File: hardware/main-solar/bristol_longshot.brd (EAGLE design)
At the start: 14 x 64 mm, 72 parts, among them U1 SAM_D20E, U2 SI4060, U3 UBLOX_MAX, U4 S25FS-S, U44 AD8354, U5 TG-5006CJ, U6 TG-5006CJ, U7 TPS3123, U8 SN74LVC1G32DCKR, U9 SE880, Y1 ABS05

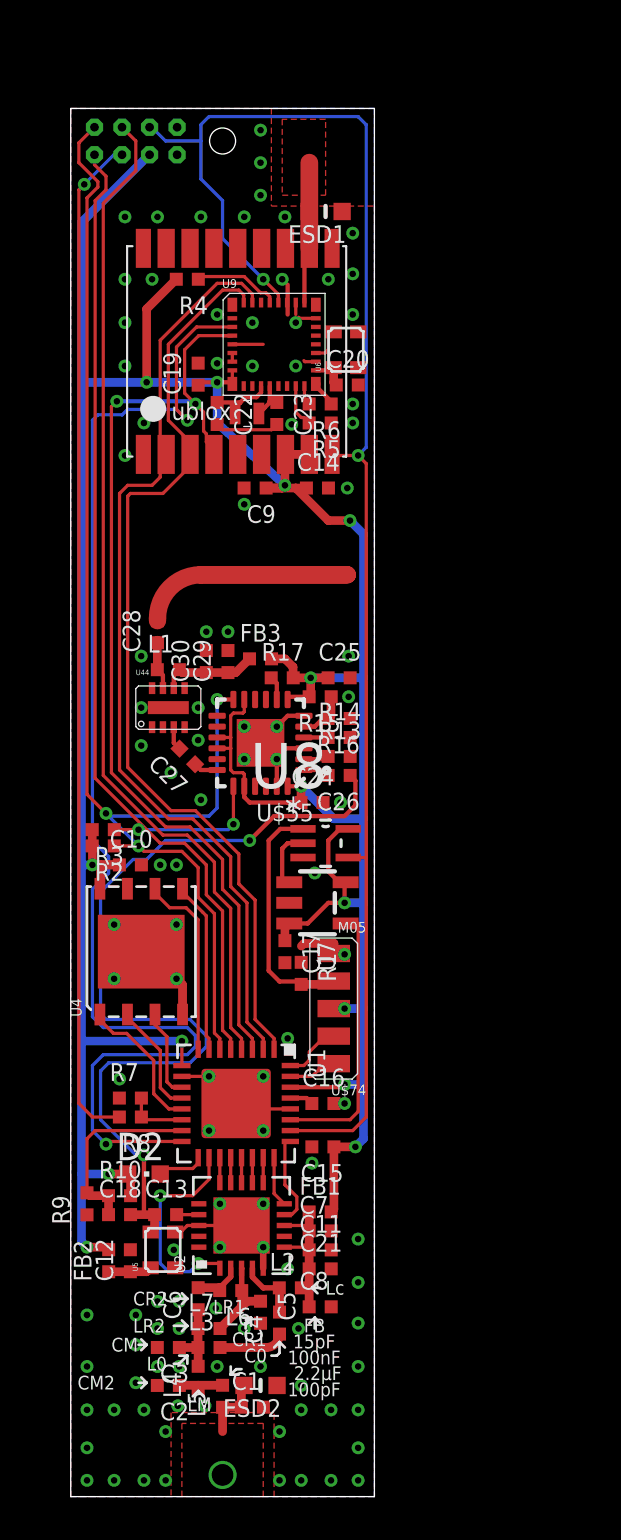
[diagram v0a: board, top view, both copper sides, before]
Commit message: Moved to single-board solar tracker. Parts lists out of date!
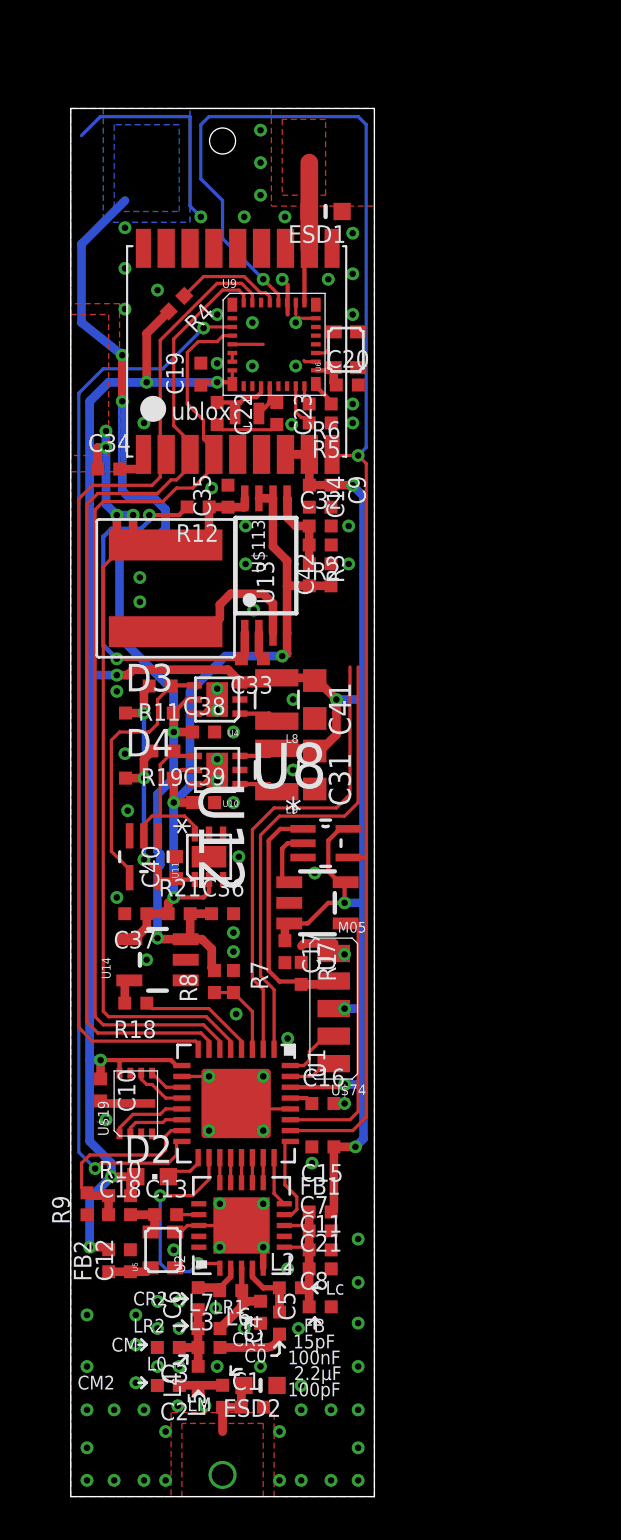
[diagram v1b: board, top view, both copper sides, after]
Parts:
- removed C24, C25, C26, C27, C28, C29: 100nF, microbuilder_v3:_0402
- removed C30: 100pF, microbuilder_v3:_0402
- removed FB3: (no value), microbuilder_v3:_0402
- removed L1: 100nH, microbuilder_v3:_0402
- removed R13, R14: 0Ω, microbuilder_v3:_0402
- removed R15, R17: 10kΩ, microbuilder_v3:_0402
- removed R16: 15kΩ, microbuilder_v3:_0402
- removed U$51: M04X2, fbri:M04X2
- removed U$55: SI5356, si5356:QFN24_4MM
- removed U44: AD8354, fbri:LFCSP_VD_8
- added C31, C41: 10µF, resistor:C0603K
- added C32, C33, C40: 1nF, microbuilder_v3:_0402
- added C34, C35, C36, C37, C38, C39, C42: 4.7µF, microbuilder_v3:_0402
- added D3, D4: BAT760, BAT760:SOD323
- added L8, L9: 2.2µH, SparkFun:1007
- added R11, R19: 10kΩ, microbuilder_v3:_0402
- added R12: 1kΩ, microbuilder_v3:_0402
- added R18: 2.2kΩ, microbuilder_v3:_0402
- added R21: DNP, microbuilder_v3:_0402
- added U$113: XAL6060, XAL6060:XAL60
- added U$19: SST25WF040BT-40I/NP, fbri:USON-8
- added U10: TPS62243, TPS62243:S-PWSON-N6
- added U11: TPS3808, TPS3808:S-PWSON-N6
- added U12: 74LVC1G04GW, 74LVC1G04GW_inverter:SOT65P210X110-5N
- added U13: SPV1040, spv1040:TSSOP8
- added U14: LT4054ES5-4.2, XYKlib:SOT23-5
- R2: value 10kΩ -> 82kΩ
- R3: value 10kΩ -> 220kΩ
- U4: value S25FS-S -> TPS62243; device fbri:WSON8 -> TPS62243:S-PWSON-N6
- moved R2 17.1 mm to (11.5, 43.9)
- moved R3 15.1 mm to (11.0, 42.5), turned to 270 degrees
- moved U4 12.1 mm to (6.75, 36.8)
- moved C10 10.5 mm to (1.38, 18.8), turned to 270 degrees
- moved R8 7.35 mm to (6.62, 23.8), turned to 90 degrees
- moved R7 7.17 mm to (7.50, 23.8), turned to 270 degrees
- moved C9 3.52 mm to (12.0, 46.1), turned to 270 degrees
- moved R4 1.23 mm to (4.88, 55.0), turned to 225 degrees
- moved C14 0.53 mm to (11.0, 46.1), turned to 270 degrees
- moved D2 0.40 mm to (3.75, 14.8)
- moved C19 0.12 mm to (6.00, 51.8)
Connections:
- net N$2 renamed SE_VREG
- net N$4 renamed SE_MODE_PULL
- net TANK renamed RF_TANK
- removed net 1.2V: R8.2, U$51.P$5
- removed net AMPL_OUT: C28.1, L1.1, U44.7
- removed net AMPL_VPOS: C29.1, C30.1, FB3.1, L1.2, U44.6
- removed net CLKIN: R14.1, U$55.4
- removed net HF_ANT: C28.2
- removed net HF_CLK: C27.1, U$55.18
- removed net INPT: C27.2, U44.3
- removed net INTR: R17.1, U$55.8
- removed net N$7: U$55.9
- removed net SSC_DIS: R15.1, R16.2, U$55.5
- removed net XA: C26.2, U$55.1
- removed net XB: R13.1, U$55.2
- new net BATTERY: C36.1, C38.1, D3.A, R21.2, R8.2, U14.3, U4.5
- new net BATTERY_BUCK_SW: L8.1, U4.1
- new net BATTERY_EN: R11.1, U12.4, U4.4
- new net CHG_CONTROL: R18.1, U1.4
- new net CHG_STATUS: U14.1
- new net CT: U11.3
- new net LX1: U$113.P$2, U13.3
- new net MPP-SET: C33.2, R12.2, U13.1
- new net MPPT-VOUT-TANK: C37.1, C39.1, C42.1, D4.A, R21.1, R3.2, U10.5, U11.2, U13.4, U13.6, U13.7, U14.4
- new net PROG: R18.2, U14.5
- new net SPV_VCTRL1: C32.1, R2.2, R3.1, U13.5
- new net SUPERVISOR_VCC: C40.1, D3.C, D4.C, R11.2, R19.2, U11.1, U12.5
- new net TANK_BUCK_SW: L9.1, U10.1
- new net TANK_EN: R19.1, U10.4, U11.6, U12.2
- net !RESET: no longer U$51.P$4
- net 1.8V: now also C31.1, C41.1, L8.2, L9.2, U$19.8, U10.3, U4.3; no longer C24.1, C25.1, FB3.2, R15.2, R17.2, R2.2, R3.2, U$51.P$3, U$55.11, U$55.15, U$55.16, U$55.20, U$55.24, U$55.7, U4.8
- net GIMO: now also U1.7; no longer U1.1
- net GND: now also C31.2, C32.2, C33.1, C34.2, C35.2, C36.2, C37.2, C38.2, C39.2, C40.2, C41.2, C42.2, R2.1, U$19.4, U$19.P$9, U10.2, U10.6, U10.PAD, U11.5, U11.PAD, U12.3, U13.2, U14.2, U4.2, U4.6; no longer C24.2, C25.2, C29.2, C30.2, R13.2, R14.2, R16.1, U$51.P$1, U$51.P$2, U$55.23, U$55.3, U$55.6, U$55.PAD, U4.4, U44.1, U44.4, U44.5, U44.8, U44.EPAD
- net GOMI: now also U1.8; no longer U1.2
- net MEM_CSN: now also U$19.1; no longer U4.1
- net MEM_MISO: now also U$19.2, U1.14; no longer U1.12, U4.2
- net MEM_MOSI: now also U$19.5, U1.11; no longer U1.7, U4.5
- net MEM_SCK: now also U$19.6, U1.12; no longer U1.8, U4.6
- net MEM_WPN: now also U$19.3; no longer U1.11, U4.3
- net SCL: now also U1.2; no longer R2.1, U$51.P$8, U$55.12, U1.6
- net SDA: now also U1.1; no longer R3.1, U$51.P$7, U$55.19, U1.5
- net TCXO_OUT: no longer C26.1
- net TIMEPULSE: now also U1.6; no longer U1.3
- net VBATT_SENSE: now also U1.3; no longer U1.14
- net VSOLAR: now also C34.1, C35.1, R12.1, U$113.P$1, U1.5, U13.8; no longer U$51.P$6, U1.4
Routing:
- net BATTERY: track 0.00 -> 49.3 mm, vias 0 -> 4
- net 1.2V: track 46.9 -> 0.00 mm, vias 1 -> 0
- net TCXO_OUT: track 41.8 -> 2.48 mm, vias 2 -> 0
- net SCL: track 59.1 -> 21.4 mm, vias 3 -> 0
- net MPPT-VOUT-TANK: track 0.00 -> 34.0 mm, vias 0 -> 3
- net SDA: track 52.6 -> 21.5 mm, vias 2 -> 0
- net 1.8V: track 166.2 -> 136.6 mm, vias 14 -> 12
- net MPP-SET: track 0.00 -> 17.5 mm, vias 0 -> 2
- net HF_ANT: track 16.4 -> 0.00 mm
- net SUPERVISOR_VCC: track 0.00 -> 14.1 mm, vias 0 -> 3
- net BATTERY_EN: track 0.00 -> 12.2 mm
- net SE_ON_OFF: track 57.6 -> 49.3 mm
- net TANK_EN: track 0.00 -> 8.03 mm
- net LX1: track 0.00 -> 7.58 mm
- net MEM_SCK: track 8.96 -> 2.51 mm
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- added copper zone on layer 16, net BATTERY
- added copper zone on layer 1, net VSOLAR
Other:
- board text added: "+vbat"
- board text added: "-vbat"
- board text added: "V0.981.0"
- board text removed: "V0.98.0"

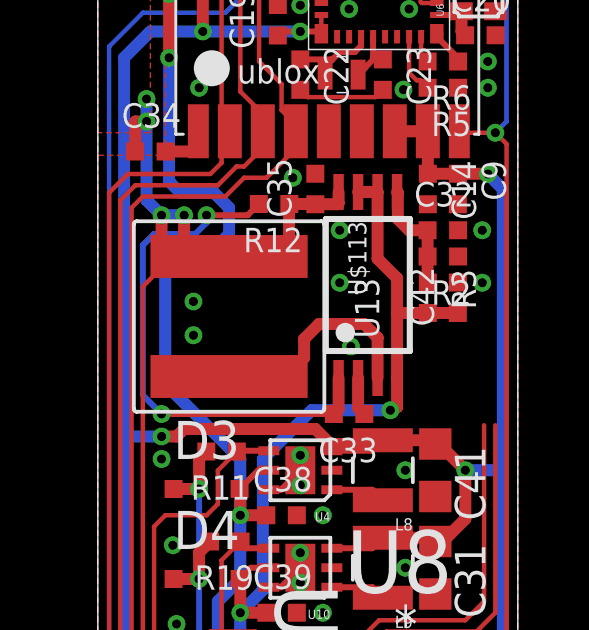
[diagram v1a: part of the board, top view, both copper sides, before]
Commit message: Added LPS3015 mppt inductor footprint alongside XAL6060 footprint
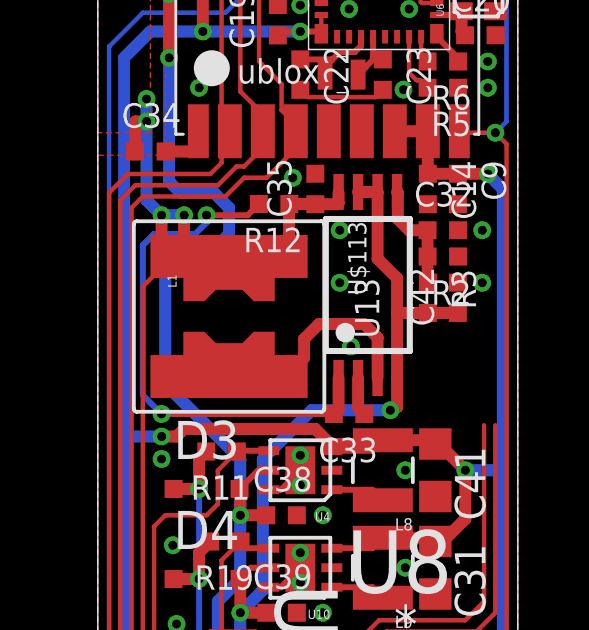
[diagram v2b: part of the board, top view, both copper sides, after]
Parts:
- added L1: 10uH LPS3015, PecanFemto4:LPS3015
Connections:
- net LX1: now also L1.2_1, L1.2_2, L1.2_3, L1.2_4, L1.2_5, L1.2_6, L1.2_7, L1.2_8, L1.2_9
- net VSOLAR: now also L1.1_1, L1.1_2, L1.1_3, L1.1_4, L1.1_5, L1.1_6, L1.1_7, L1.1_8, L1.1_9
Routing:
- net LX1: track 7.58 -> 12.8 mm
- net VSOLAR: track 47.9 -> 52.6 mm
- net GND: vias 107 -> 105
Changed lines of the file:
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@@
 <setting verticaltext="up"/>
 </settings>
-<grid distance="0.125" unitdist="mm" unit="mm" style="lines" multiple="1" display="yes" altdistance="0.025" altunitdist="inch" altunit="inch"/>
+<grid distance="1" unitdist="mm" unit="mm" style="lines" multiple="1" display="yes" altdistance="0.025" altunitdist="inch" altunit="inch"/>
 <layers>
 <layer number="1" name="Top" color="4" fill="1" visible="yes" active="yes"/>
@@
 <layer number="54" name="bGND_GNDA" color="1" fill="9" visible="no" active="no"/>
 <layer number="56" name="wert" color="7" fill="1" visible="no" active="no"/>
+<layer number="57" name="tCAD" color="7" fill="1" visible="no" active="no"/>
 <layer number="90" name="Modules" color="5" fill="1" visible="no" active="no"/>
 <layer number="91" name="Nets" color="2" fill="1" visible="no" active="no"/>
@@
 <layer number="97" name="Info" color="7" fill="1" visible="no" active="no"/>
 <layer number="98" name="Guide" color="6" fill="1" visible="no" active="no"/>
+<layer number="99" name="SpiceOrder" color="7" fill="1" visible="no" active="no"/>
 <layer number="100" name="Muster" color="7" fill="1" visible="no" active="no"/>
 <layer number="101" name="Patch_Top" color="12" fill="4" visible="yes" active="yes"/>
@@
 <layer number="132" name="bAdjust" color="7" fill="1" visible="yes" active="yes"/>
 <layer number="144" name="Drill_legend" color="7" fill="1" visible="yes" active="yes"/>
+<layer number="150" name="Notes" color="7" fill="1" visible="yes" active="yes"/>
 <layer number="151" name="HeatSink" color="7" fill="1" visible="yes" active="yes"/>
 <layer number="152" name="_bDocu" color="7" fill="1" visible="yes" active="yes"/>
+<layer number="153" name="FabDoc1" color="7" fill="1" visible="yes" active="yes"/>
+<layer number="154" name="FabDoc2" color="7" fill="1" visible="yes" active="yes"/>
+<layer number="155" name="FabDoc3" color="7" fill="1" visible="yes" active="yes"/>
 <layer number="199" name="Contour" color="7" fill="1" visible="yes" active="yes"/>
 <layer number="200" name="200bmp" color="1" fill="10" visible="yes" active="yes"/>
@@
 <element name="C42" library="microbuilder_v3" package="_0402" value="4.7µF" x="12" y="42.5" rot="R90"/>
 <element name="R21" library="microbuilder_v3" package="_0402" value="DNP" x="5" y="26.875"/>
+<element name="L1" library="PecanFemto4" package="LPS3015" value="10uH LPS3015" x="4.375" y="41.875" rot="R270"/>
 </elements>
 <signals>
@@
 <via x="8.0625" y="44.75" extent="1-16" drill="0.3"/>
 <via x="8.0625" y="43" extent="1-16" drill="0.3"/>
-<via x="3.1875" y="42.375" extent="1-16" drill="0.3"/>
-<via x="3.1875" y="41.25" extent="1-16" drill="0.3"/>
 <via x="8.4375" y="40.875" extent="1-16" drill="0.3"/>
 <wire x1="5.5" y1="63.625" x2="1.375" y2="63.625" width="0.15" layer="16"/>
@@
 <wire x1="6.375" y1="45.617" x2="6.375" y2="44" width="0.4" layer="1"/>
 <wire x1="6.375" y1="44" x2="6.25" y2="43.875" width="0.4" layer="1"/>
-<wire x1="6.25" y1="43.875" x2="4.375" y2="43.875" width="0.4" layer="1"/>
+<wire x1="6.25" y1="43.875" x2="6" y2="43.875" width="0.4" layer="1"/>
+<wire x1="6" y1="43.875" x2="4.375" y2="43.875" width="0.4" layer="1"/>
 <wire x1="7.25" y1="45.617" x2="7.992" y2="45.617" width="0.4" layer="1"/>
 <wire x1="7.992" y1="45.617" x2="8.025" y2="45.65" width="0.4" layer="1"/>
@@
 <vertex x="0" y="48"/>
 </polygon>
+<contactref element="L1" pad="1_5"/>
+<contactref element="L1" pad="1_6"/>
+<contactref element="L1" pad="1_9"/>
+<contactref element="L1" pad="1_8"/>
+<contactref element="L1" pad="1_3"/>
+<contactref element="L1" pad="1_2"/>
+<contactref element="L1" pad="1_1"/>
+<contactref element="L1" pad="1_4"/>
+<contactref element="L1" pad="1_7"/>
+<wire x1="4.375" y1="43.875" x2="4.375" y2="43.145" width="0.2" layer="1"/>
+<wire x1="5.75" y1="43.375" x2="5.75" y2="42.8495" width="0.2" layer="1"/>
+<wire x1="5.75" y1="42.8495" x2="5.772" y2="42.8275" width="0.2" layer="1"/>
+<wire x1="5.772" y1="42.8275" x2="5.261459375" y2="42.8275" width="0.2" layer="1"/>
+<wire x1="5.261459375" y1="42.8275" x2="5.197959375" y2="42.764" width="0.2" layer="1"/>
+<wire x1="5.42275" y1="42.5735" x2="5.388459375" y2="42.5735" width="0.2" layer="1"/>
+<wire x1="5.388459375" y1="42.5735" x2="5.197959375" y2="42.764" width="0.2" layer="1"/>
+<wire x1="5.6457625" y1="43.2727625" x2="5.6457625" y2="43.5207625" width="0.2" layer="1"/>
+<wire x1="5.6457625" y1="43.5207625" x2="6" y2="43.875" width="0.2" layer="1"/>
+<wire x1="2.875" y1="43.625" x2="2.875" y2="43.502" width="0.2" layer="1"/>
+<wire x1="2.875" y1="43.502" x2="3.1042375" y2="43.2727625" width="0.2" layer="1"/>
+<wire x1="3.1042375" y1="43.2727625" x2="3.1042375" y2="42.9537375" width="0.2" layer="1"/>
+<wire x1="3.1042375" y1="42.9537375" x2="2.978" y2="42.8275" width="0.2" layer="1"/>
+<wire x1="2.978" y1="42.8275" x2="3.07325" y2="42.8275" width="0.2" layer="1"/>
+<wire x1="3.07325" y1="42.8275" x2="3.32725" y2="42.5735" width="0.2" layer="1"/>
+<wire x1="3.32725" y1="42.5735" x2="3.361540625" y2="42.5735" width="0.2" layer="1"/>
+<wire x1="3.361540625" y1="42.5735" x2="3.552040625" y2="42.764" width="0.2" layer="1"/>
 </signal>
 <signal name="VBATT_SENSE">
@@
 <wire x1="6.375" y1="40" x2="4.5" y2="40" width="0.4" layer="1"/>
 <wire x1="4.5" y1="40" x2="4.375" y2="39.875" width="0.4" layer="1"/>
+<contactref element="L1" pad="2_1"/>
+<contactref element="L1" pad="2_2"/>
+<contactref element="L1" pad="2_3"/>
+<contactref element="L1" pad="2_5"/>
+<contactref element="L1" pad="2_8"/>
+<contactref element="L1" pad="2_6"/>
+<contactref element="L1" pad="2_4"/>
+<contactref element="L1" pad="2_7"/>
+<contactref element="L1" pad="2_9"/>
+<wire x1="2.978" y1="40.9225" x2="2.978" y2="40.978" width="0.2" layer="1"/>
+<wire x1="2.978" y1="40.978" x2="3" y2="41" width="0.2" layer="1"/>
+<wire x1="2.978" y1="40.9225" x2="2.978" y2="40.603475" width="0.2" layer="1"/>
+<wire x1="2.978" y1="40.603475" x2="3.1042375" y2="40.4772375" width="0.2" layer="1"/>
+<wire x1="3" y1="41" x2="3.15075" y2="41" width="0.2" layer="1"/>
+<wire x1="3.15075" y1="41" x2="3.32725" y2="41.1765" width="0.2" layer="1"/>
+<wire x1="3.552040625" y1="40.986" x2="3.933040625" y2="40.605" width="0.2" layer="1"/>
+<wire x1="3.933040625" y1="40.605" x2="4.375" y2="40.605" width="0.2" layer="1"/>
+<wire x1="3.32725" y1="41.1765" x2="3.51775" y2="40.986" width="0.2" layer="1"/>
+<wire x1="3.51775" y1="40.986" x2="3.552040625" y2="40.986" width="0.2" layer="1"/>
+<wire x1="4.375" y1="40.605" x2="4.375" y2="39.875" width="0.2" layer="1"/>
+<wire x1="5.42275" y1="41.1765" x2="5.67675" y2="40.9225" width="0.2" layer="1"/>
+<wire x1="5.67675" y1="40.9225" x2="5.772" y2="40.9225" width="0.2" layer="1"/>
+<wire x1="5.772" y1="40.9225" x2="5.6457625" y2="40.7962625" width="0.2" layer="1"/>
+<wire x1="5.6457625" y1="40.7962625" x2="5.6457625" y2="40.4772375" width="0.2" layer="1"/>
+<wire x1="6.375" y1="40" x2="5.8977625" y2="40.4772375" width="0.2" layer="1"/>
+<wire x1="5.8977625" y1="40.4772375" x2="5.6457625" y2="40.4772375" width="0.2" layer="1"/>
+<wire x1="5.42275" y1="41.1765" x2="5.23225" y2="40.986" width="0.2" layer="1"/>
+<wire x1="5.23225" y1="40.986" x2="5.197959375" y2="40.986" width="0.2" layer="1"/>
 </signal>
 <signal name="MPP-SET">
